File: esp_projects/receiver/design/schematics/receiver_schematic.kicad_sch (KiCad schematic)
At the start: 4 parts, among them U2 STM32L432KCUx, U3 TB6612FNG, U4 TB6612FNG, U5 XIAO-ESP32-C3-DIP

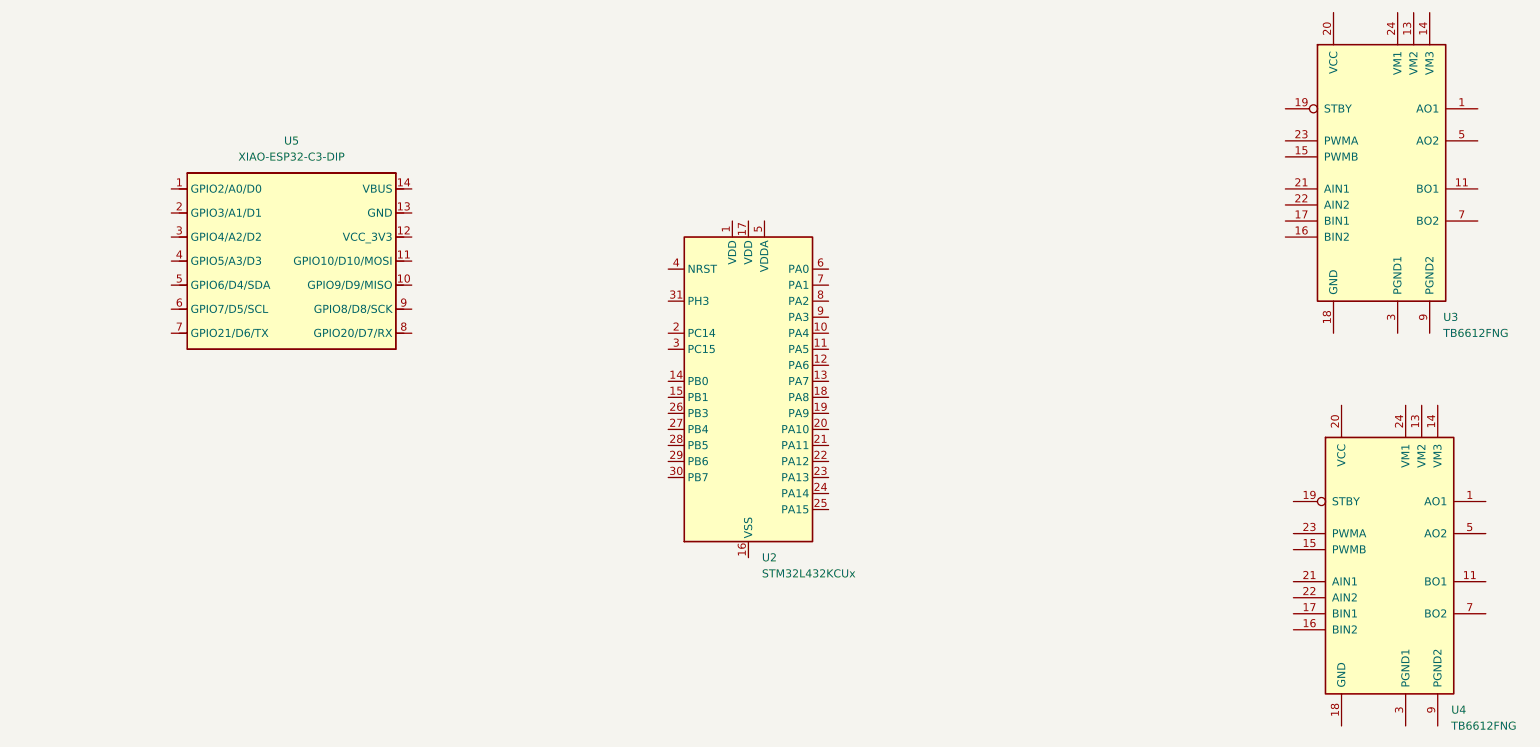
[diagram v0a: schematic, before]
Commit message: Update schematics and backup archives
Switch paper size from A4 to USLetter for consistency
Updates align with version revision to 1.0.1
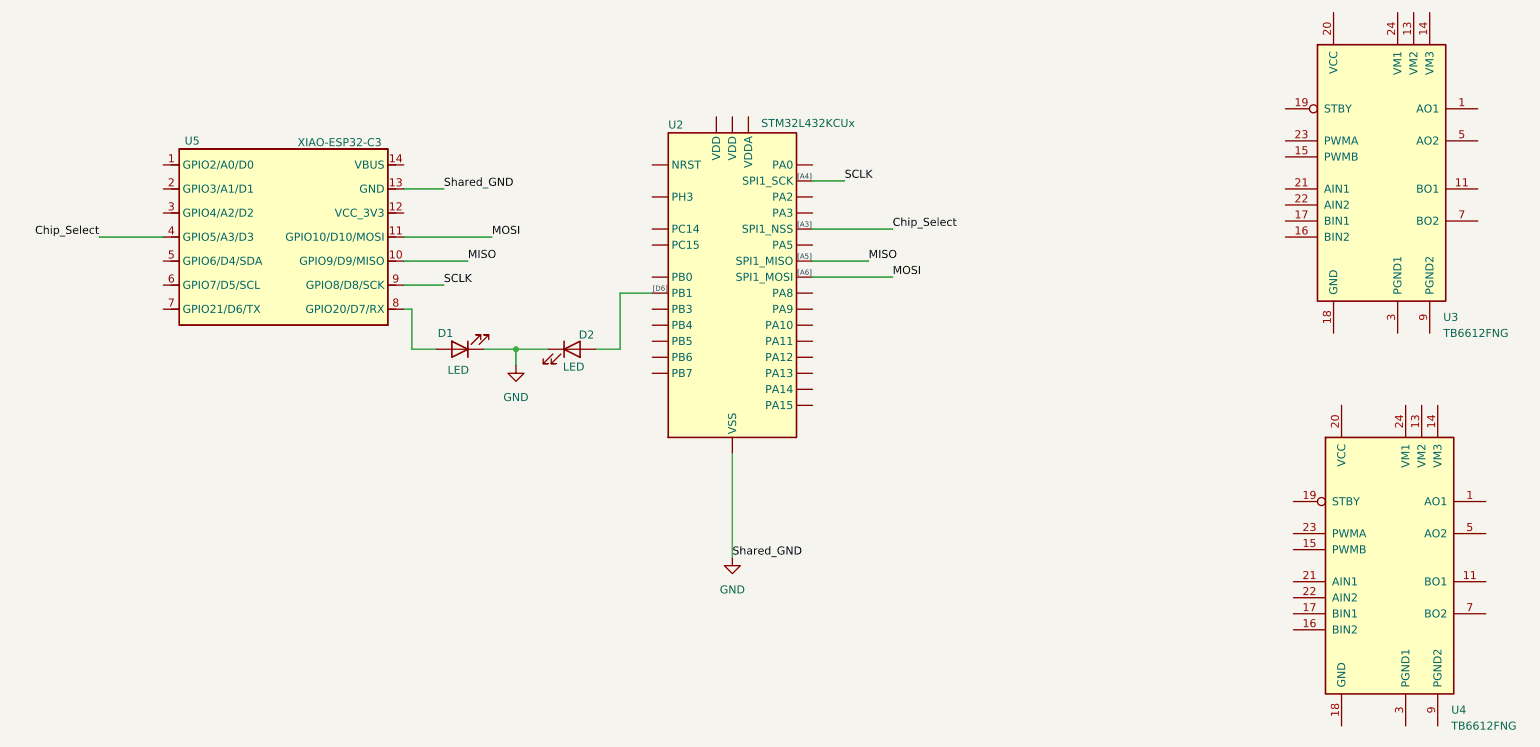
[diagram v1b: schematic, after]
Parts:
- added D1, D2: LED, symbol Device:LED
- U5: value XIAO-ESP32-C3-DIP -> XIAO-ESP32-C3
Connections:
- net MISO: now reaches U5.10 (GPIO9/D9/MISO)
- net MISO: now also U2.12 (PA6)
- net MOSI: now reaches U5.11 (GPIO10/D10/MOSI)
- net MOSI: now also U2.13 (PA7)
- net GND: now reaches U5.13 (GND)
- net GND: now also U2.16 (VSS), U2.32 (VSS), U2.33 (VSS), D1.1 (K), D2.1 (K)
- net Chip_Select: now reaches U5.4 (GPIO5/A3/D3)
- net Chip_Select: now also U2.10 (PA4)
- net at U5.8 (GPIO20/D7/RX): now also D1.2 (A)
- net SCLK: now reaches U5.9 (GPIO8/D8/SCK)
- net SCLK: now also U2.7 (PA1)
- net at U2.15 (PB1): now also D2.2 (A)
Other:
- note added: "[A3]"
- note added: "[A4]"
- note added: "[A5]"
- note added: "[A6]"
- note added: "[D6]"
- moved on the sheet: U5

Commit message: Corrects annotation reference in schematic
Updates the annotation from [A4] to [A1] on the
receiver schematic to reflect the correct reference
designation. This change ensures accuracy in schematic
documentation and aligns with the intended design layout.
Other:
- note added: "[A1]"
- note removed: "[A4]"
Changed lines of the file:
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@@
 		)
 	)
-	(text "[A4]\n"
+	(text "[A1]"
 		(exclude_from_sim no)
 		(at 139.7 55.372 0)
